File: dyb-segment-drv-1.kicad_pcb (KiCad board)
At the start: 2 copper layers, 76 x 76 mm, 192 parts, among them J1 Conn_01x10, Q1 HL2300, Q10 HL2300, Q11 HL2300, Q12 HL2300, Q13 HL2300, Q14 HL2300, Q15 HL2300, Q16 HL2300, Q2 HL2300, Q3 HL2300, Q4 HL2300, Q5 HL2300, Q6 HL2300, Q7 HL2300, Q8 HL2300, Q9 HL2300, SW1 SW_SPDT, U1 AP2112K-1.8, U10 74AUC2G32, U11 74AUC2G32, U12 74AUC2G32, U13 74AUC2G32, U14 74AUC2G32, U15 Inverter_Schmitt_Dual, U16 Inverter_Schmitt_Dual, U17 SN74AUP2G08, U18 SN74AUP2G08, U19 SN74AUP2G08, U2 GS3911AG, U20 SN74AUP2G08, U21 SN74AUP2G08, U22 74AUC2G32, U23 74AUC2G32, U24 74AUC2G32, U25 74AUC2G32, U26 74AUC2G32, U27 GS3911AG, U28 SN74AUP2G08, U29 SN74AUP2G08, U3 SN74AUP2G08, U30 SN74AUP2G08, U31 SN74AUP2G08, U32 SN74AUP2G08, U33 SN74AUP2G08, U34 74AUC2G32, U35 74AUC2G32, U36 74AUC2G32, U37 74AUC2G32, U38 74AUC2G32, U39 74AUC2G32, U4 SN74AUP2G08, U40 Inverter_Schmitt_Dual, U41 Inverter_Schmitt_Dual, U42 SN74AUP2G08, U43 SN74AUP2G08, U44 SN74AUP2G08, U45 SN74AUP2G08, U46 SN74AUP2G08, U47 74AUC2G32, U48 74AUC2G32, U49 74AUC2G32, U5 SN74AUP2G08, U50 74AUC2G32, U51 74AUC2G32, U6 SN74AUP2G08, U7 SN74AUP2G08, U8 SN74AUP2G08, U9 74AUC2G32

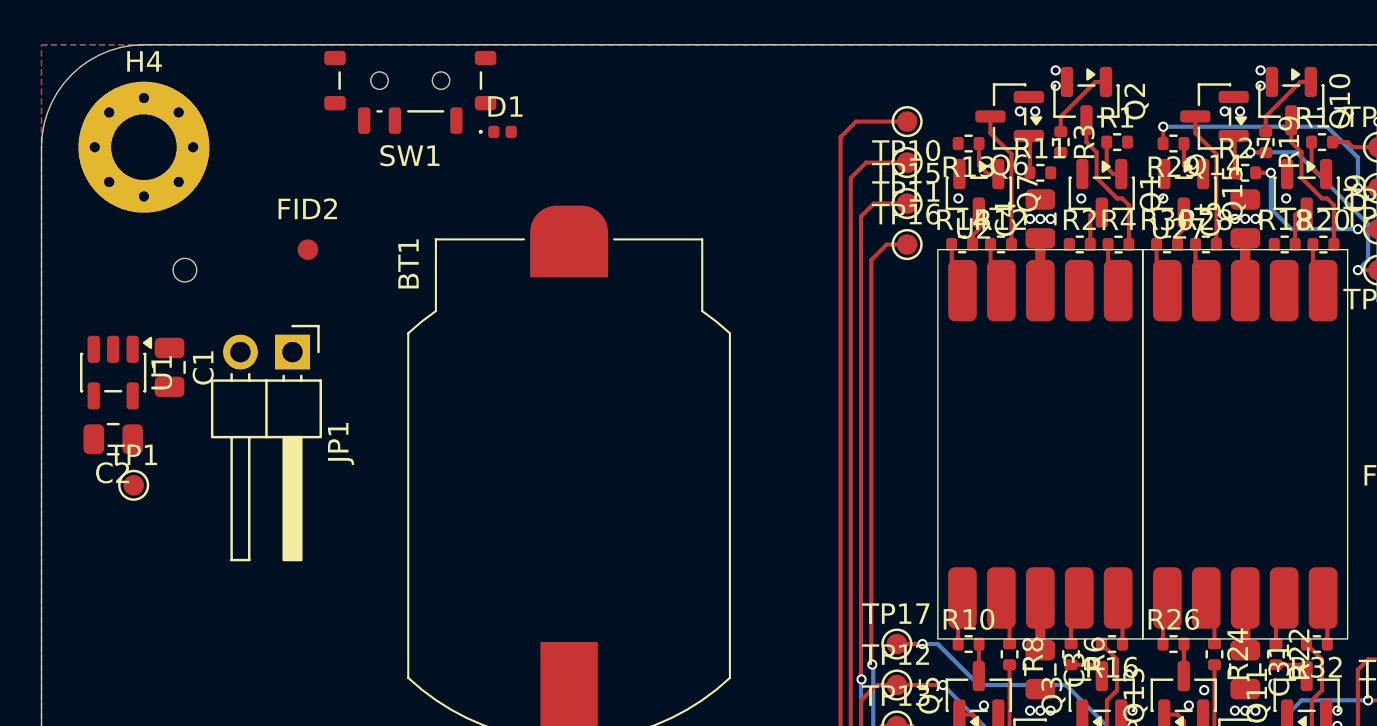
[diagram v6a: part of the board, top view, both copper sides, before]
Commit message: pcb: route +batt
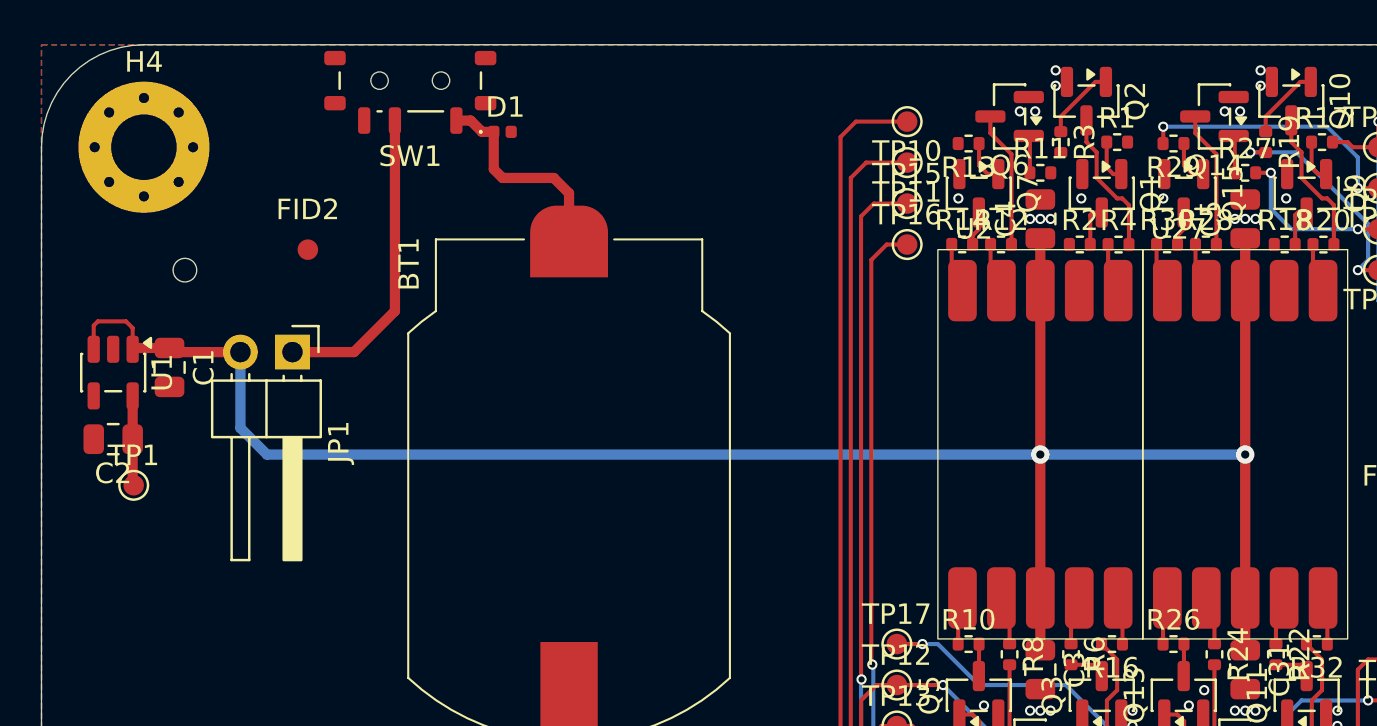
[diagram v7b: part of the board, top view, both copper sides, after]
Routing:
- net +BATT: track 10.2 -> 118.3 mm, vias 0 -> 2
- net Net-(BT1-+): track 0.00 -> 10.5 mm
- net +1V8: track 0.00 -> 4.38 mm
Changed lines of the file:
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@@
 	)
 	(segment
+		(start 114.45 38.25)
+		(end 114.45 40.45)
+		(width 0.5)
+		(layer "F.Cu")
+		(net "+1V8")
+	)
+	(segment
+		(start 114.45 36.1375)
+		(end 114.45 38.25)
+		(width 0.5)
+		(layer "F.Cu")
+		(net "+1V8")
+	)
+	(segment
+		(start 114.45 40.45)
+		(end 114.5 40.5)
+		(width 0.5)
+		(layer "F.Cu")
+		(net "+1V8")
+	)
+	(segment
 		(start 167.35 63.75)
 		(end 168.25 63.75)
@@
 	)
 	(segment
+		(start 127.25 22.7)
+		(end 127.25 32)
+		(width 0.5)
+		(layer "F.Cu")
+		(net "+BATT")
+	)
+	(segment
+		(start 127.25 32)
+		(end 125.25 34)
+		(width 0.5)
+		(layer "F.Cu")
+		(net "+BATT")
+	)
+	(segment
 		(start 158.75 28.45)
 		(end 158.75 31)
@@
 	)
 	(segment
+		(start 116.25 33.8)
+		(end 114.5125 33.8)
+		(width 0.5)
+		(layer "F.Cu")
+		(net "+BATT")
+	)
+	(segment
+		(start 168.75 39)
+		(end 168.75 31)
+		(width 0.5)
+		(layer "F.Cu")
+		(net "+BATT")
+	)
+	(segment
+		(start 168.75 46)
+		(end 168.75 39)
+		(width 0.5)
+		(layer "F.Cu")
+		(net "+BATT")
+	)
+	(segment
+		(start 114.125 32.5)
+		(end 114.45 32.825)
+		(width 0.2)
+		(layer "F.Cu")
+		(net "+BATT")
+	)
+	(segment
+		(start 125.25 34)
+		(end 122.25 34)
+		(width 0.5)
+		(layer "F.Cu")
+		(net "+BATT")
+	)
+	(segment
+		(start 114.5125 33.8)
+		(end 114.45 33.8625)
+		(width 0.5)
+		(layer "F.Cu")
+		(net "+BATT")
+	)
+	(segment
+		(start 112.75 32.5)
+		(end 114.125 32.5)
+		(width 0.2)
+		(layer "F.Cu")
+		(net "+BATT")
+	)
+	(segment
+		(start 112.55 33.8625)
+		(end 112.55 32.7)
+		(width 0.2)
+		(layer "F.Cu")
+		(net "+BATT")
+	)
+	(segment
+		(start 114.45 32.825)
+		(end 114.45 33.8625)
+		(width 0.2)
+		(layer "F.Cu")
+		(net "+BATT")
+	)
+	(segment
 		(start 158.75 48.55)
 		(end 158.75 46)
@@
 	)
 	(segment
+		(start 119.71 34)
+		(end 116.45 34)
+		(width 0.5)
+		(layer "F.Cu")
+		(net "+BATT")
+	)
+	(segment
+		(start 112.55 32.7)
+		(end 112.75 32.5)
+		(width 0.2)
+		(layer "F.Cu")
+		(net "+BATT")
+	)
+	(segment
+		(start 158.75 31)
+		(end 158.75 39)
+		(width 0.5)
+		(layer "F.Cu")
+		(net "+BATT")
+	)
+	(segment
+		(start 158.75 39)
+		(end 158.75 46)
+		(width 0.5)
+		(layer "F.Cu")
+		(net "+BATT")
+	)
+	(segment
 		(start 168.75 28.45)
 		(end 168.75 31)
@@
 	)
 	(segment
+		(start 116.45 34)
+		(end 116.25 33.8)
+		(width 0.5)
+		(layer "F.Cu")
+		(net "+BATT")
+	)
+	(segment
 		(start 168.75 48.55)
 		(end 168.75 46)
@@
 		(net "+BATT")
 	)
+	(via
+		(at 158.75 39)
+		(size 0.9)
+		(drill 0.4)
+		(layers "F.Cu" "B.Cu")
+		(net "+BATT")
+	)
+	(via
+		(at 168.75 39)
+		(size 0.9)
+		(drill 0.4)
+		(layers "F.Cu" "B.Cu")
+		(net "+BATT")
+	)
+	(segment
+		(start 119.71 34)
+		(end 119.71 37.71)
+		(width 0.5)
+		(layer "B.Cu")
+		(net "+BATT")
+	)
+	(segment
+		(start 158.75 39)
+		(end 168.75 39)
+		(width 0.5)
+		(layer "B.Cu")
+		(net "+BATT")
+	)
+	(segment
+		(start 119.71 37.71)
+		(end 121 39)
+		(width 0.5)
+		(layer "B.Cu")
+		(net "+BATT")
+	)
+	(segment
+		(start 121 39)
+		(end 158.75 39)
+		(width 0.5)
+		(layer "B.Cu")
+		(net "+BATT")
+	)
 	(segment
 		(start 167.25 48.24)
@@
 	)
 	(segment
+		(start 130.95 22.7)
+		(end 130.25 22.7)
+		(width 0.5)
+		(layer "F.Cu")
+		(net "Net-(BT1-+)")
+	)
+	(segment
+		(start 135.75 28.75)
+		(end 135.75 26.25)
+		(width 0.5)
+		(layer "F.Cu")
+		(net "Net-(BT1-+)")
+	)
+	(segment
+		(start 132.5 25.5)
+		(end 132.075 25.075)
+		(width 0.5)
+		(layer "F.Cu")
+		(net "Net-(BT1-+)")
+	)
+	(segment
+		(start 135 25.5)
+		(end 132.5 25.5)
+		(width 0.5)
+		(layer "F.Cu")
+		(net "Net-(BT1-+)")
+	)
+	(segment
+		(start 132.075 25.075)
+		(end 132.075 23.25)
+		(width 0.5)
+		(layer "F.Cu")
+		(net "Net-(BT1-+)")
+	)
+	(segment
+		(start 132.075 23.25)
+		(end 131.5 23.25)
+		(width 0.5)
+		(layer "F.Cu")
+		(net "Net-(BT1-+)")
+	)
+	(segment
+		(start 135.75 26.25)
+		(end 135 25.5)
+		(width 0.5)
+		(layer "F.Cu")
+		(net "Net-(BT1-+)")
+	)
+	(segment
+		(start 131.5 23.25)
+		(end 130.95 22.7)
+		(width 0.5)
+		(layer "F.Cu")
+		(net "Net-(BT1-+)")
+	)
+	(segment

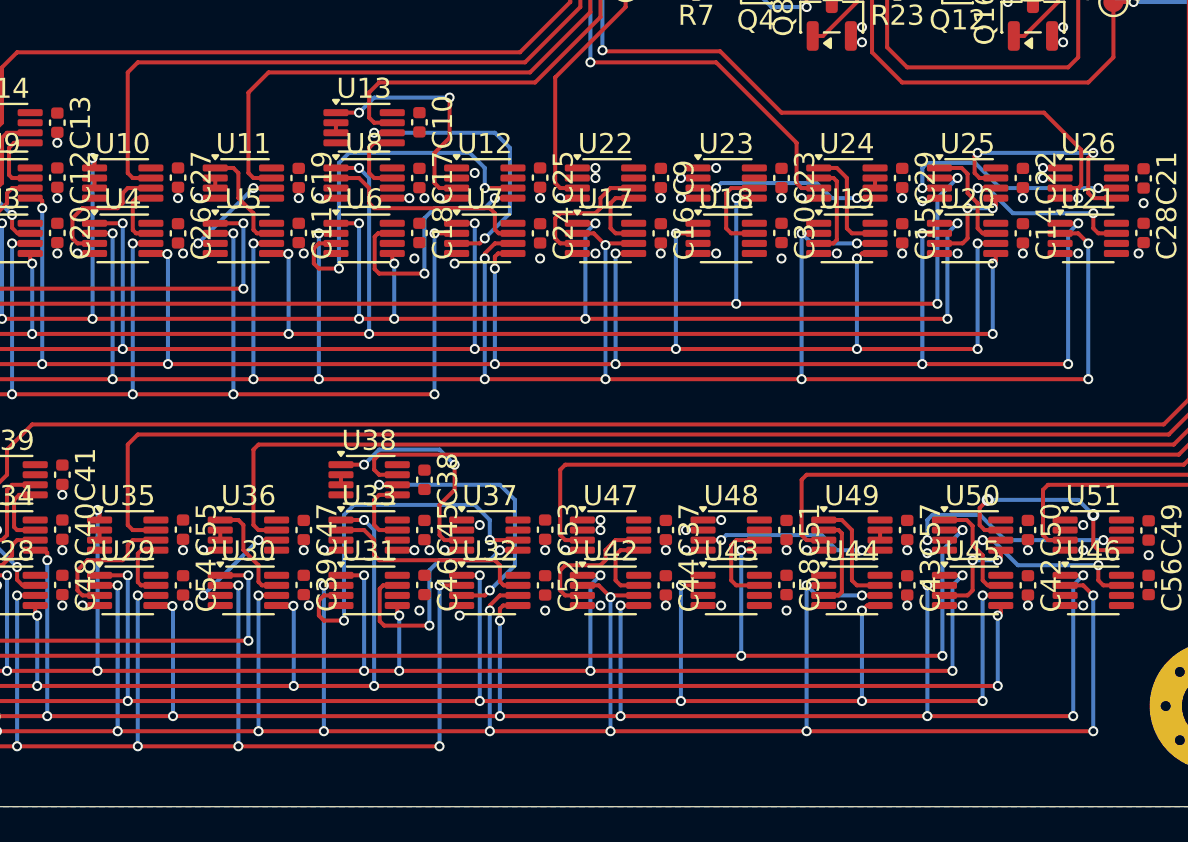
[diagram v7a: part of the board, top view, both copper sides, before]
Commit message: pcb: route missing gates connections
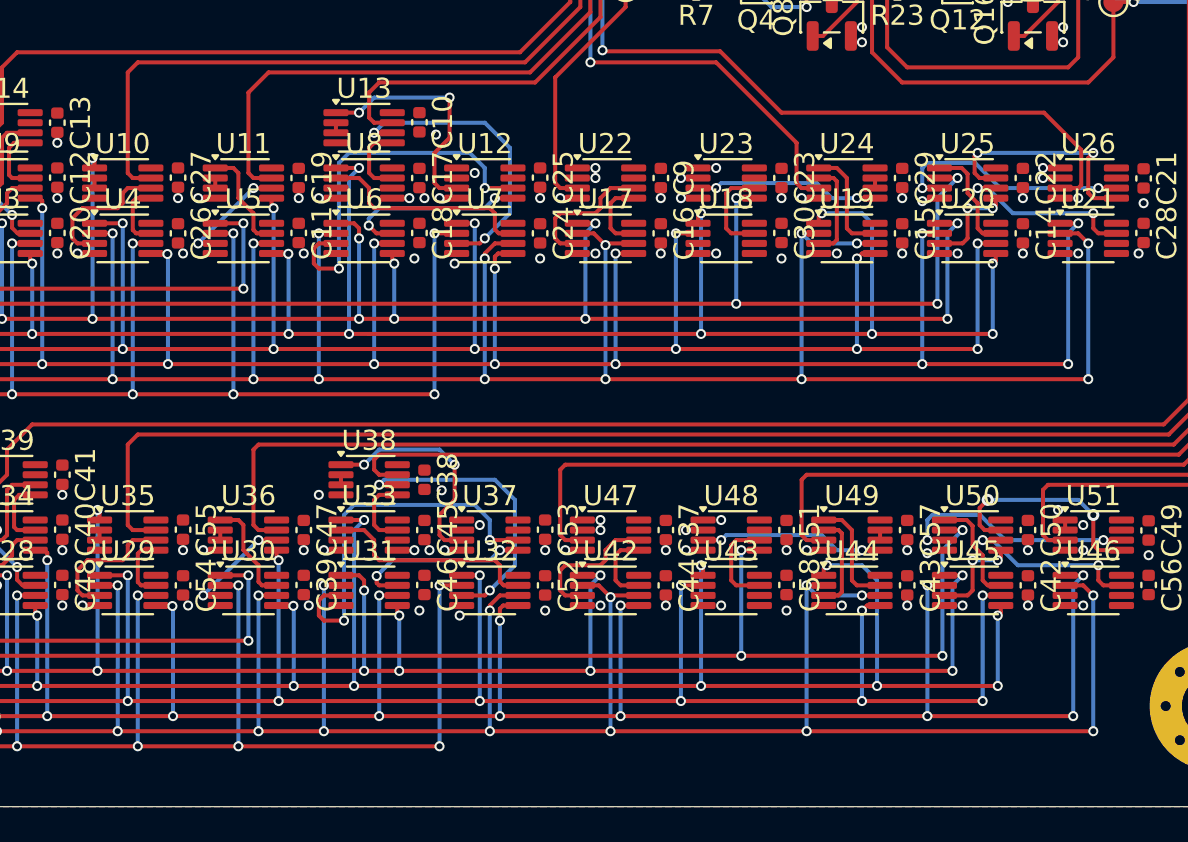
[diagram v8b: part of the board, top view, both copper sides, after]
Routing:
- net /A1: track 76.5 -> 91.8 mm, vias 8 -> 12
- net /B1: track 76.5 -> 91.7 mm, vias 8 -> 12
- net /Segment Driver1/~{D2}: track 88.9 -> 96.4 mm, vias 10 -> 12
- net /Segment Driver/~{D2}: track 88.9 -> 96.4 mm, vias 10 -> 12
- net /B2: track 101.1 -> 108.0 mm, vias 12 -> 14
- net /A2: track 101.1 -> 108.0 mm, vias 12 -> 14
- net Net-(U31-Pad7): track 12.7 -> 8.98 mm
- net Net-(U12-Pad5): track 12.7 -> 9.26 mm
- net GND: track 0.00 -> 0.50 mm, vias 139 -> 143
